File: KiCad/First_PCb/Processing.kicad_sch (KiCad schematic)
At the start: 10 parts, among them J4 Conn_01x02_Pin, U5 ESP32-DEVKITC-32D, U8 74HCT244D

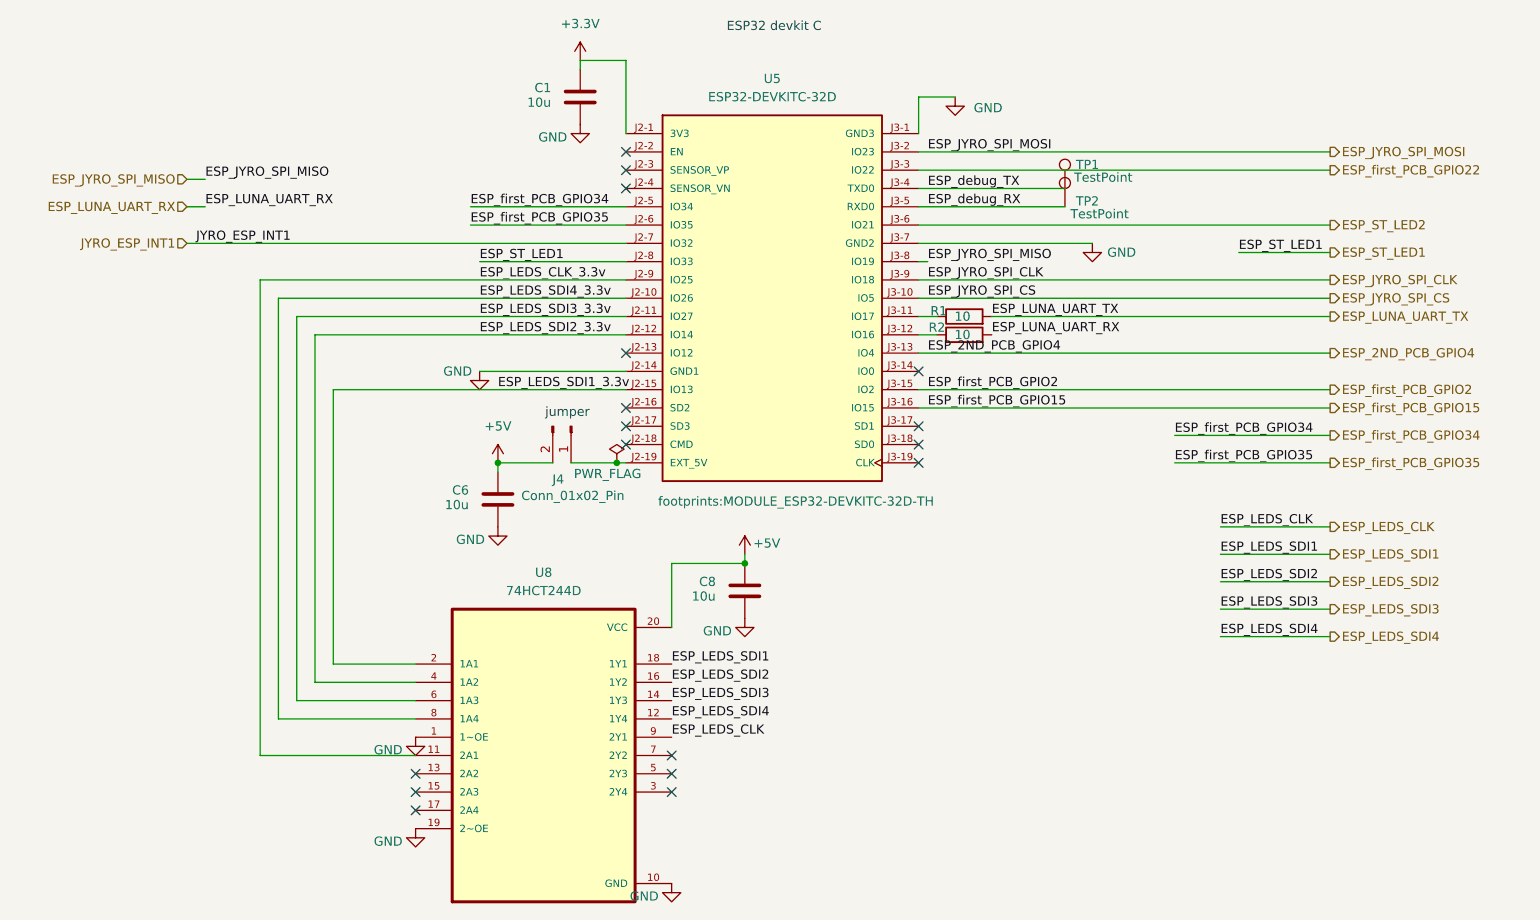
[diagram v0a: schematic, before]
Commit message: added all the kicad files & gerbers of the first pcb
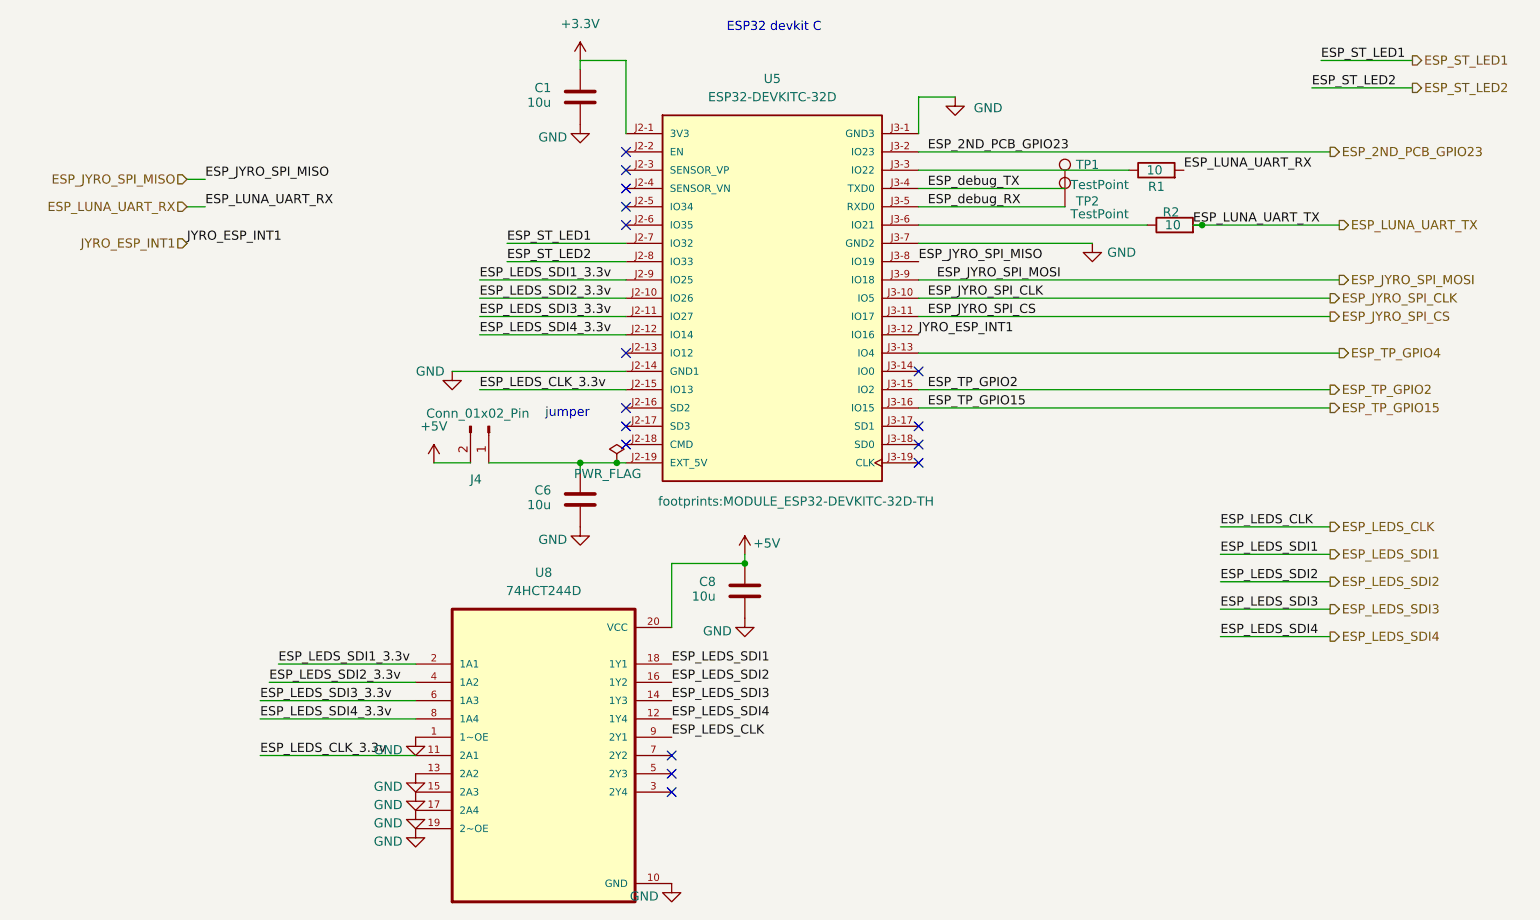
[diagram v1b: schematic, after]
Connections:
- net ESP_first_PCB_GPIO22 is gone; now on an unnamed net: U5.J3-3 (IO22)
- net +5V: no longer C6.1
- net ESP_JYRO_SPI_CLK: now also U5.J3-10 (IO5); no longer U5.J3-9 (IO18)
- net ESP_JYRO_SPI_CS: now also U5.J3-11 (IO17); no longer U5.J3-10 (IO5)
- net ESP_JYRO_SPI_MOSI: now also U5.J3-9 (IO18); no longer U5.J3-2 (IO23)
- net ESP_LEDS_CLK_3.3v: now also U5.J2-15 (IO13); no longer U5.J2-9 (IO25)
- net ESP_LEDS_SDI1_3.3v: now also U5.J2-9 (IO25); no longer U5.J2-15 (IO13)
- net ESP_LEDS_SDI2_3.3v: now also U5.J2-10 (IO26); no longer U5.J2-12 (IO14)
- net ESP_LEDS_SDI4_3.3v: now also U5.J2-12 (IO14); no longer U5.J2-10 (IO26)
- net ESP_LUNA_UART_RX: now also R1.2; no longer R2.2
- net ESP_LUNA_UART_TX: now also R2.2; no longer R1.2
- net ESP_ST_LED1: now also U5.J2-7 (IO32); no longer U5.J2-8 (IO33)
- net ESP_ST_LED2: now also U5.J2-8 (IO33); no longer U5.J3-6 (IO21)
- net GND: now also U8.13 (2A2), U8.15 (2A3), U8.17 (2A4)
- net JYRO_ESP_INT1: now also U5.J3-12 (IO16); no longer U5.J2-7 (IO32)
- net at R2.1: now also U5.J3-6 (IO21); no longer U5.J3-12 (IO16)
- net at R1.1: no longer U5.J3-11 (IO17)
- net at J4.1 (Pin_1), U5.J2-19 (EXT_5V): now also C6.1
- net ESP_2ND_PCB_GPIO4 renamed ESP_TP_GPIO4
- net ESP_first_PCB_GPIO15 renamed ESP_TP_GPIO15
- net ESP_first_PCB_GPIO2 renamed ESP_TP_GPIO2
- net ESP_first_PCB_GPIO34: no longer names the net of U5.J2-5 (IO34)
- net ESP_first_PCB_GPIO35: no longer names the net of U5.J2-6 (IO35)
- new net ESP_2ND_PCB_GPIO23: U5.J3-2 (IO23)
- no-connect marks 17 -> 16
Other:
- moved on the sheet: C6, J4, R1, R2
